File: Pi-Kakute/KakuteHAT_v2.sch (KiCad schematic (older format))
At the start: 52 parts, among them J100 FC_Socket, J101 FC_Socket2, J102 Polulu_socket, J103 Conn_01x01, J11 Mout3_4, J12 I2C, J13 ID_EEPROM, J20 Power_Pad, J3 40HAT, J5 RC_IN, J6 GPS2, J8 Mout1_2, Q1 DMG2305UX, Q2 DMMT5401, SW1 Kakute Power Switch, SW2 Pi Power Switch, U3 D24V22F5, U4 AP2204RA-3.3, U5 NC7SZ00P5X, U6 KakuteF4_V2, U7 TPS54331DR, U8 TPS22810

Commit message: Pi-Kakute: Import and clean-up from KakuteHat folder
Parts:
- removed J102: Polulu_socket, Connector_PinHeader_2.54mm:PinHeader_1x05_P2.54mm_Vertical, symbol Connector_Generic:Conn_01x05
- removed J103: Conn_01x01, Connector_PinHeader_2.54mm:PinHeader_1x01_P2.54mm_Vertical, symbol Connector_Generic:Conn_01x01
- removed J12: I2C, OPL_Connector:H2-2.54, symbol OPL_Connector:DIP-BLACK-MALE-HEADER-VERT_2P-2.54_
- removed SW1: Kakute Power Switch, OPL_Switch:SW5-2.0-8.8X4.4X4.7MM-90D, symbol OPL_Switch:DIP-TOGGLE-SWITCH-ON-ON_3+2P-8.8X4.6MM_-90D
- removed U3: D24V22F5, Polulu:D24V22F5_NoPin, symbol Polulu:D24V22F5
- added J3: I2C, Connector_PinHeader_2.54mm:PinHeader_1x02_P2.54mm_Vertical, symbol Connector_Generic:Conn_01x02
- added SW1: Pi Power Switch, Button_Switch_THT:SW_CuK_OS102011MA1QN1_SPDT_Angled, symbol Switch:SW_SPDT
- C1: renamed from C10; footprint OPL_Capacitor:C0402 -> Capacitor_SMD:C_0402_1005Metric; symbol OPL_Capacitor:CERAMIC-100NF-50V-10%-X7R_0603_ -> Device:C
- C10: renamed from C14; footprint Resistor_SMD:R_0402_1005Metric -> Capacitor_SMD:C_0402_1005Metric
- C11: renamed from C15; footprint Resistor_SMD:R_0402_1005Metric -> Capacitor_SMD:C_0402_1005Metric
- C2: renamed from C9; footprint OPL_Capacitor:C0402 -> Capacitor_SMD:C_0402_1005Metric; symbol OPL_Capacitor:CERAMIC-100NF-50V-10%-X7R_0603_ -> Device:C
- C3: renamed from C17; footprint 0805 -> Capacitor_SMD:C_0805_2012Metric; symbol SparkFun-Capacitors:1.0UF-0805-25V-10% -> Device:C
- C4: renamed from C5; footprint 0805 -> Capacitor_SMD:C_0805_2012Metric; symbol SparkFun-Capacitors:1.0UF-0805-25V-10% -> Device:C
- C5: renamed from C13; footprint OPL_Capacitor:C0402 -> Capacitor_SMD:C_0402_1005Metric
- C6: renamed from C16; footprint Resistor_SMD:R_1206_3216Metric_Pad1.42x1.75mm_HandSolder -> Capacitor_SMD:C_1206_3216Metric
- C7: renamed from C6; footprint 0805 -> Capacitor_SMD:C_0805_2012Metric; symbol SparkFun-Capacitors:1.0UF-0805-25V-10% -> Device:C
- C8: renamed from C11; footprint OPL_Capacitor:C0402 -> Capacitor_SMD:C_0402_1005Metric; symbol OPL_Capacitor:CERAMIC-100NF-50V-10%-X7R_0603_ -> Device:C
- C9: renamed from C12; footprint Capacitor_SMD:C_1210_3225Metric_Pad1.42x2.65mm_HandSolder -> Capacitor_SMD:C_1210_3225Metric
- D2: renamed from D1; footprint OPL_Discrete_Semiconductor:SOD-123 -> Diode_SMD:D_SOD-123; symbol OPL_Discrete_Semiconductor:SMD-DIODE-100V-200MA_SOD-123_ -> Device:D
- R1: renamed from R6; footprint OPL_Resistor:R0603 -> Resistor_SMD:R_0603_1608Metric; symbol OPL_Resistor:SMD-RES-3.9K-5%-1_10W_0603_ -> Device:R
- R10: renamed from R17; symbol OPL_Resistor:SMD-RES-0.1R-5%-1_8W_0805_ -> Device:R
- R2: renamed from R8; footprint OPL_Resistor:R0603 -> Resistor_SMD:R_0603_1608Metric; symbol OPL_Resistor:SMD-RES-3.9K-5%-1_10W_0603_ -> Device:R
- R3: renamed from R23; footprint OPL_Resistor:R0603 -> Resistor_SMD:R_0603_1608Metric; symbol OPL_Resistor:SMD-RES-10K-5%-1_10W_0603_ -> Device:R
- R4: renamed from R24; footprint OPL_Resistor:R0402 -> Resistor_SMD:R_0402_1005Metric; symbol OPL_Resistor:SMD-RES-47K-5%-1_16W_0402_ -> Device:R
- R5: renamed from R18; footprint OPL_Resistor:R0603 -> Resistor_SMD:R_0603_1608Metric; symbol OPL_Resistor:SMD-RES-10K-5%-1_10W_0603_ -> Device:R
- R6: renamed from R11; footprint OPL_Resistor:R0603 -> Resistor_SMD:R_0603_1608Metric; symbol OPL_Resistor:SMD-RES-3.9K-5%-1_10W_0603_ -> Device:R
- R7: renamed from R10; footprint OPL_Resistor:R0603 -> Resistor_SMD:R_0603_1608Metric; symbol OPL_Resistor:SMD-RES-3.9K-5%-1_10W_0603_ -> Device:R
- R8: renamed from R15; footprint OPL_Resistor:R0603 -> Resistor_SMD:R_0603_1608Metric; symbol OPL_Resistor:SMD-RES-47K-5%-1_16W_0402_ -> Device:R
- R9: renamed from R16; footprint OPL_Resistor:R0402 -> Resistor_SMD:R_0402_1005Metric; symbol OPL_Resistor:SMD-RES-47K-5%-1_16W_0402_ -> Device:R
- SW2: footprint OPL_Switch:SW5-2.0-8.8X4.4X4.7MM-90D -> Button_Switch_THT:SW_CuK_OS102011MA1QN1_SPDT_Angled; symbol OPL_Switch:DIP-TOGGLE-SWITCH-ON-ON_3+2P-8.8X4.6MM_-90D -> Switch:SW_SPDT
- renumbered D3 to D1, D2 to D3, H5 to H1, H1 to H2, H2 to H4, H4 to H5, J3 to J1, J100 to J12, J13 to J2, J8 to J4, J11 to J5, J5 to J6, J6 to J7, J20 to J8, J101 to J9, Q2 to Q1, Q1 to Q2, U8 to U1, U4 to U2, U6 to U3, U7 to U4
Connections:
- wire segments 169 -> 159

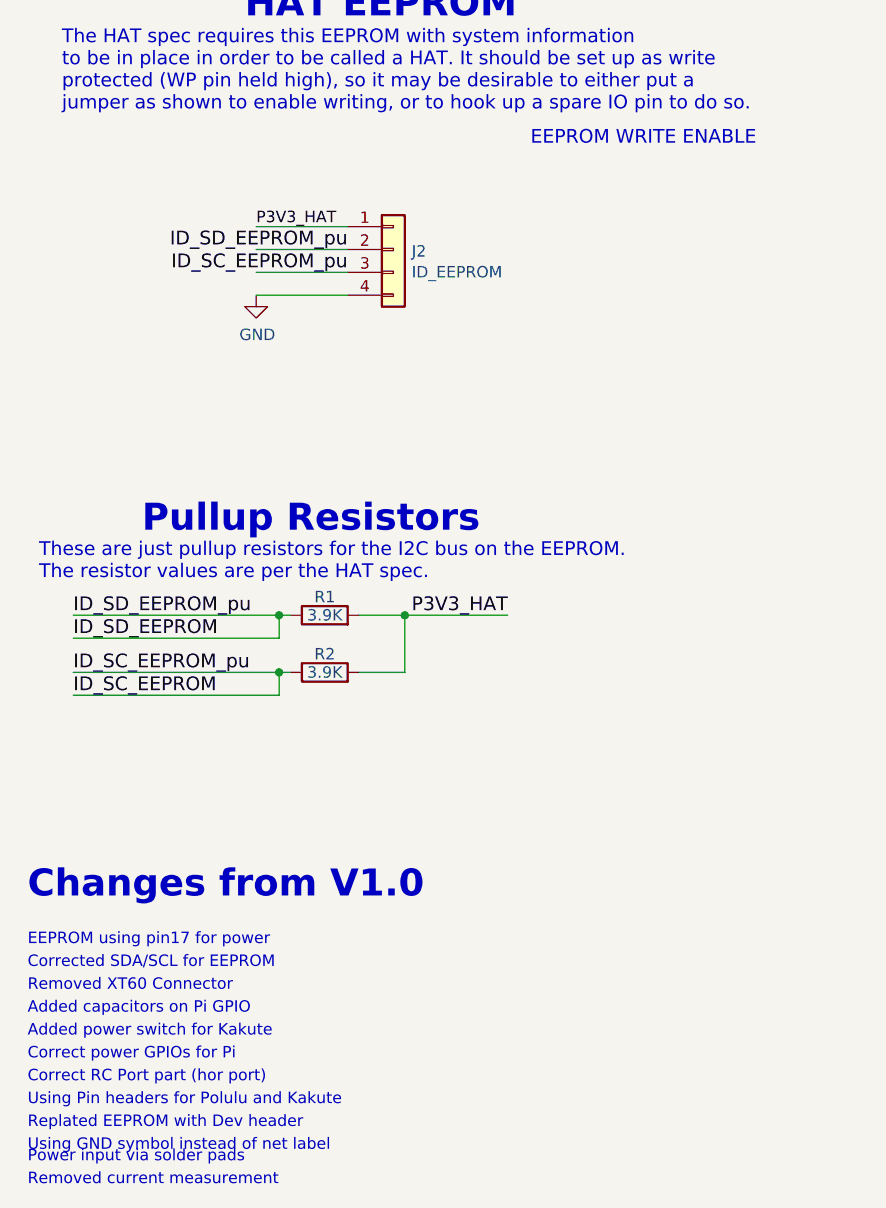
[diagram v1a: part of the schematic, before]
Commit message: Pi-Kakute: Added EEPROM and improved 40-pin header and mounting holes
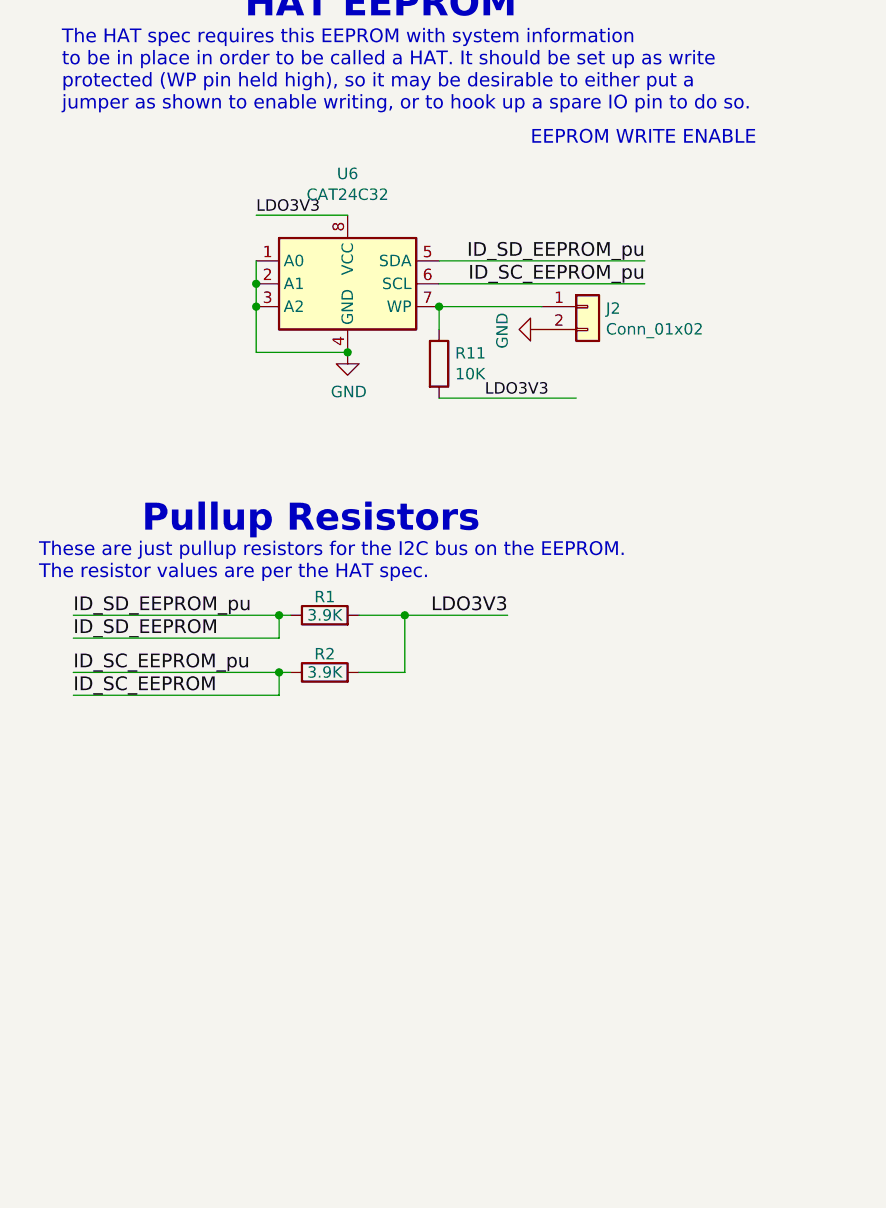
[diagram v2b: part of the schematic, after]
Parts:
- removed J2: ID_EEPROM, Connector_PinHeader_2.54mm:PinHeader_1x04_P2.54mm_Vertical, symbol Connector_Generic:Conn_01x04
- added J2: Conn_01x02, Connector_PinHeader_2.54mm:PinHeader_1x02_P2.54mm_Vertical, symbol Connector_Generic:Conn_01x02
- added R11: 10K, Resistor_SMD:R_0603_1608Metric, symbol Device:R
- added U6: CAT24C32, Package_SO:SOIC-8_3.9x4.9mm_P1.27mm, symbol Memory_EEPROM:CAT24C256
- H2, H3, H4, H5: footprint project_footprints:NPTH_3mm_ID -> MountingHole:MountingHole_3.2mm_M3_ISO7380
- J1: MFR Adafruit -> Sullins Connector Solutions; MPN 1979 -> PPPC202LFBN-RC; SPN 1528-1783-ND -> S7123-ND
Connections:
- wire segments 159 -> 165
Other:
- note removed: "Added capacitors on Pi GPIO"
- note removed: "Added power switch for Kakute"
- note removed: "Changes from V1.0"
- note removed: "Correct RC Port part (hor port)"
- note removed: "Correct power GPIOs for Pi"
- note removed: "Corrected SDA/SCL for EEPROM"
- note removed: "EEPROM using pin17 for power"
- note removed: "Power input via solder pads"
- note removed: "Removed XT60 Connector"
- note removed: "Removed current measurement"
- note removed: "Replated EEPROM with Dev header"
- note removed: "Using GND symbol instead of net label"
- note removed: "Using Pin headers for Polulu and Kakute"
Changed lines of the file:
@@
 EESchema Schematic File Version 4
 LIBS:KakuteHAT_v2-cache
+LIBS:PiConnectLite-cache
 EELAYER 29 0
 EELAYER END
@@
 F 0 "H2" H 5500 6100 60  0000 C CNN
 F 1 "3mm_Mounting_Hole" H 5650 5850 60  0000 C CNN
-F 2 "project_footprints:NPTH_3mm_ID" H 5550 6000 60  0001 C CNN
+F 2 "MountingHole:MountingHole_3.2mm_M3_ISO7380" H 5550 6000 60  0001 C CNN
 F 3 "" H 5550 6000 60  0001 C CNN
 F 4 "~" H 0   0   50  0001 C CNN "MFR"
@@
 F 0 "H4" H 6500 6100 60  0000 C CNN
 F 1 "3mm_Mounting_Hole" H 6650 5850 60  0000 C CNN
-F 2 "project_footprints:NPTH_3mm_ID" H 6550 6000 60  0001 C CNN
+F 2 "MountingHole:MountingHole_3.2mm_M3_ISO7380" H 6550 6000 60  0001 C CNN
 F 3 "" H 6550 6000 60  0001 C CNN
 F 4 "~" H 0   0   50  0001 C CNN "MFR"
@@
 F 0 "H3" H 5500 6650 60  0000 C CNN
 F 1 "3mm_Mounting_Hole" H 5650 6400 60  0000 C CNN
-F 2 "project_footprints:NPTH_3mm_ID" H 5550 6550 60  0001 C CNN
+F 2 "MountingHole:MountingHole_3.2mm_M3_ISO7380" H 5550 6550 60  0001 C CNN
 F 3 "" H 5550 6550 60  0001 C CNN
 F 4 "~" H 0   0   50  0001 C CNN "MFR"
@@
 F 0 "H5" H 6550 6650 60  0000 C CNN
 F 1 "3mm_Mounting_Hole" H 6700 6400 60  0000 C CNN
-F 2 "project_footprints:NPTH_3mm_ID" H 6600 6550 60  0001 C CNN
+F 2 "MountingHole:MountingHole_3.2mm_M3_ISO7380" H 6600 6550 60  0001 C CNN
 F 3 "" H 6600 6550 60  0001 C CNN
 F 4 "~" H 0   0   50  0001 C CNN "MFR"
@@
 F 2 "Connector_PinSocket_2.54mm:PinSocket_2x20_P2.54mm_Vertical" H 2650 3300 50  0001 C CNN
 F 3 "" H 1950 3100 50  0000 C CNN
-F 4 "Adafruit" H 50  850 50  0001 C CNN "MFR"
-F 5 "1979" H 50  850 50  0001 C CNN "MPN"
-F 6 "1528-1783-ND" H 50  850 50  0001 C CNN "SPN"
+F 4 "Sullins Connector Solutions" H 50  850 50  0001 C CNN "MFR"
+F 5 "PPPC202LFBN-RC" H 50  850 50  0001 C CNN "MPN"
+F 6 "S7123-ND" H 50  850 50  0001 C CNN "SPN"
 F 7 "Digikey" H 50  850 50  0001 C CNN "SPR"
 	1    2650 3100
@@
 $EndComp
 Text Label 3150 7400 2    60   ~ 0
-P3V3_HAT
+LDO3V3
 Text Label 7150 2400 2    60   ~ 0
 P5V_HAT
@@
 Text Notes 8950 2500 0    118  ~ 24
 Power Input and Current Measure
-Text Notes 1050 8650 0    118  ~ 24
-Changes from V1.0
-Text Notes 1050 8850 0    50   ~ 0
-EEPROM using pin17 for power
-Text Notes 1050 8950 0    50   ~ 0
-Corrected SDA/SCL for EEPROM
 Wire Wire Line
 	2750 1800 2850 1800
@@
 Wire Wire Line
 	1850 2300 1300 2300
-Text Notes 1050 9050 0    50   ~ 0
-Removed XT60 Connector
 $Comp
 L Device:C C2
@@
 Wire Wire Line
 	1350 4000 1350 4250
-Text Notes 1050 9150 0    50   ~ 0
-Added capacitors on Pi GPIO
 Wire Wire Line
 	10300 6000 10050 6000
 Text Label 10050 6000 0    50   ~ 0
 VIN_RAW
-Text Notes 1050 9250 0    50   ~ 0
-Added power switch for Kakute
-Text Notes 1050 9350 0    50   ~ 0
-Correct power GPIOs for Pi
 Connection ~ 2700 7400
 Wire Wire Line
 	4400 2900 4400 3150
-Text Notes 1050 9450 0    50   ~ 0
-Correct RC Port part (hor port)
 Wire Wire Line
 	11750 6850 12250 6850
-Text Notes 1050 9550 0    50   ~ 0
-Using Pin headers for Polulu and Kakute
-$Comp
-L Connector_Generic:Conn_01x04 J2
-U 1 1 5C4F52AC
-P 2650 5800
-F 0 "J2" H 2730 5792 50  0000 L CNN
-F 1 "ID_EEPROM" H 2730 5701 50  0000 L CNN
-F 2 "Connector_PinHeader_2.54mm:PinHeader_1x04_P2.54mm_Vertical" H 2650 5800 50  0001 C CNN
-F 3 "~" H 2650 5800 50  0001 C CNN
-F 4 "~" H 0   0   50  0001 C CNN "MFR"
-F 5 "~" H 0   0   50  0001 C CNN "MPN"
-	1    2650 5800
-	1    0    0    -1
-$EndComp
-Wire Wire Line
-	2450 5700 2050 5700
-Wire Wire Line
-	2450 5800 2050 5800
-Wire Wire Line
-	2450 5900 2050 5900
-Wire Wire Line
-	2450 6000 2050 6000
-Text Label 2050 5700 0    50   ~ 0
-P3V3_HAT
-Text Label 2450 5800 2    60   ~ 0
+Wire Wire Line
+	2450 5650 2050 5650
+Text Label 2050 5650 0    50   ~ 0
+LDO3V3
+Text Label 3750 5850 2    60   ~ 0
 ID_SD_EEPROM_pu
-Text Label 2450 5900 2    60   ~ 0
+Text Label 3750 5950 2    60   ~ 0
 ID_SC_EEPROM_pu
-Text Notes 1050 9650 0    50   ~ 0
-Replated EEPROM with Dev header
 $Comp
 L Connector_Generic:Conn_01x02 J8
@@
 L power:GND #PWR02
 U 1 1 5C6347D7
-P 2050 6000
-F 0 "#PWR02" H 2050 5750 50  0001 C CNN
-F 1 "GND" H 2055 5827 50  0000 C CNN
-F 2 "" H 2050 6000 50  0001 C CNN
-F 3 "" H 2050 6000 50  0001 C CNN
-	1    2050 6000
+P 2450 6250
+F 0 "#PWR02" H 2450 6000 50  0001 C CNN
+F 1 "GND" H 2455 6077 50  0000 C CNN
+F 2 "" H 2450 6250 50  0001 C CNN
+F 3 "" H 2450 6250 50  0001 C CNN
+	1    2450 6250
 	1    0    0    -1
 $EndComp
@@
 	1    0    0    -1
 $EndComp
-Text Notes 1050 9750 0    50   ~ 0
-Using GND symbol instead of net label
-Text Notes 1050 9800 0    50   ~ 0
-Power input via solder pads
 Wire Wire Line
 	8150 7800 9000 7800
@@
 Text Label 10450 2900 0    50   ~ 0
 VIN_RAW
-Text Notes 1050 9900 0    50   ~ 0
-Removed current measurement
 $Comp
 L Regulator_Switching:TPS54340DDA U4
@@
 	0    1    1    0
 $EndComp
+$Comp
+L Memory_EEPROM:CAT24C256 U6
+U 1 1 5DC3D434
+P 2450 5950
+F 0 "U6" H 2450 6431 50  0000 C CNN
+F 1 "CAT24C32" H 2450 6340 50  0000 C CNN
+F 2 "Package_SO:SOIC-8_3.9x4.9mm_P1.27mm" H 2450 5950 50  0001 C CNN
+F 3 "https://www.onsemi.com/pub/Collateral/CAT24C128-D.PDF" H 2450 5950 50  0001 C CNN
+F 4 "ON Semiconductor" H 2450 5950 50  0001 C CNN "MFR"
+F 5 "CAT24C32WI-GT3 " H 2450 5950 50  0001 C CNN "MPN"
+F 6 "CAT24C32WI-GT3CT-ND" H 2450 5950 50  0001 C CNN "SPN"
+F 7 "Digikey" H 2450 5950 50  0001 C CNN "SPR"
+	1    2450 5950
+	1    0    0    -1
+$EndComp
+Wire Wire Line
+	2050 5850 2050 5950
+Wire Wire Line
+	2050 5950 2050 6050
+Connection ~ 2050 5950
+Wire Wire Line
+	2050 6050 2050 6250
+Wire Wire Line
+	2050 6250 2450 6250
+Connection ~ 2050 6050
+Connection ~ 2450 6250
+Wire Wire Line
+	2850 6050 3300 6050
+Wire Wire Line
+	2850 6050 2850 6150
+Connection ~ 2850 6050
+Wire Wire Line
+	2850 5850 3750 5850
+Wire Wire Line
+	2850 5950 3750 5950
+$Comp
+L Connector_Generic:Conn_01x02 J2
+U 1 1 5DCB1EC3
+P 3500 6050
+F 0 "J2" H 3580 6042 50  0000 L CNN
+F 1 "Conn_01x02" H 3580 5951 50  0000 L CNN
+F 2 "Connector_PinHeader_2.54mm:PinHeader_1x02_P2.54mm_Vertical" H 3500 6050 50  0001 C CNN
+F 3 "~" H 3500 6050 50  0001 C CNN
+F 4 "~" H 3500 6050 50  0001 C CNN "MFR"
+F 5 "~" H 3500 6050 50  0001 C CNN "MPN"
+F 6 "~" H 3500 6050 50  0001 C CNN "SPN"
+F 7 "~" H 3500 6050 50  0001 C CNN "SPR"
+	1    3500 6050
+	1    0    0    -1
+$EndComp
+$Comp
+L power:GND #PWR0102
+U 1 1 5DCB3377
+P 3300 6150
+F 0 "#PWR0102" H 3300 5900 50  0001 C CNN
+F 1 "GND" H 3305 5977 50  0000 C CNN
+F 2 "" H 3300 6150 50  0001 C CNN
+F 3 "" H 3300 6150 50  0001 C CNN
+	1    3300 6150
+	0    1    1    0
+$EndComp
+$Comp
+L Device:R R11
+U 1 1 5DCB3A5C
+P 2850 6300
+F 0 "R11" H 2920 6346 50  0000 L CNN
+F 1 "10K" H 2920 6255 50  0000 L CNN
+F 2 "Resistor_SMD:R_0603_1608Metric" V 2780 6300 50  0001 C CNN
+F 3 "~" H 2850 6300 50  0001 C CNN
+F 4 "Yageo" H 2850 6300 50  0001 C CNN "MFR"
+F 5 "RC0603JR-0710KL" H 2850 6300 50  0001 C CNN "MPN"
+F 6 "301010293" H 2850 6300 50  0001 C CNN "SKU"
+F 7 "311-10KGRCT-ND" H 2850 6300 50  0001 C CNN "SPN"
+F 8 "OPL" H 2850 6300 50  0001 C CNN "SPR"
+	1    2850 6300
+	1    0    0    -1
+$EndComp
+Wire Wire Line
+	2850 6450 3450 6450
+Text Label 3050 6450 0    50   ~ 0
+LDO3V3
 $EndSCHEMATC
